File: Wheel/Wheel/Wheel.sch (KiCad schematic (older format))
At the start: 118 parts, among them J1 Conn_02x09_Odd_Even, J10 RJ45, J11 Screw_Terminal_01x02, J12 DS-201, J13 Conn_01x04, J14 Conn_02x13_Top_Bottom, J15 DB25_Female, J16 Conn_01x06, J17 Conn_01x07, J18 Conn_01x06, J19 RJ45, J2 RJ45, J20 DB9_Male, J21 DB9_Female, J3 RJ45, J4 RJ45, J5 USB_B, J6 Conn_02x09_Odd_Even, J7 Conn_02x10_Odd_Even, J8 RJ45, J9 RJ45, U1 MCP23S17_SP, U10 PC817, U11 PC817, U12 IP4220CZ6, U15 PC817, U2 STM32F407VETx, U3 USBLC6-2SC6, U4 IP4220CZ6, U5 MCP23S17_SP, U6 AMS1117, U7 4N35, U8 PC817, U9 PC817, Y1 32,768 кГц, Y2 8MHz

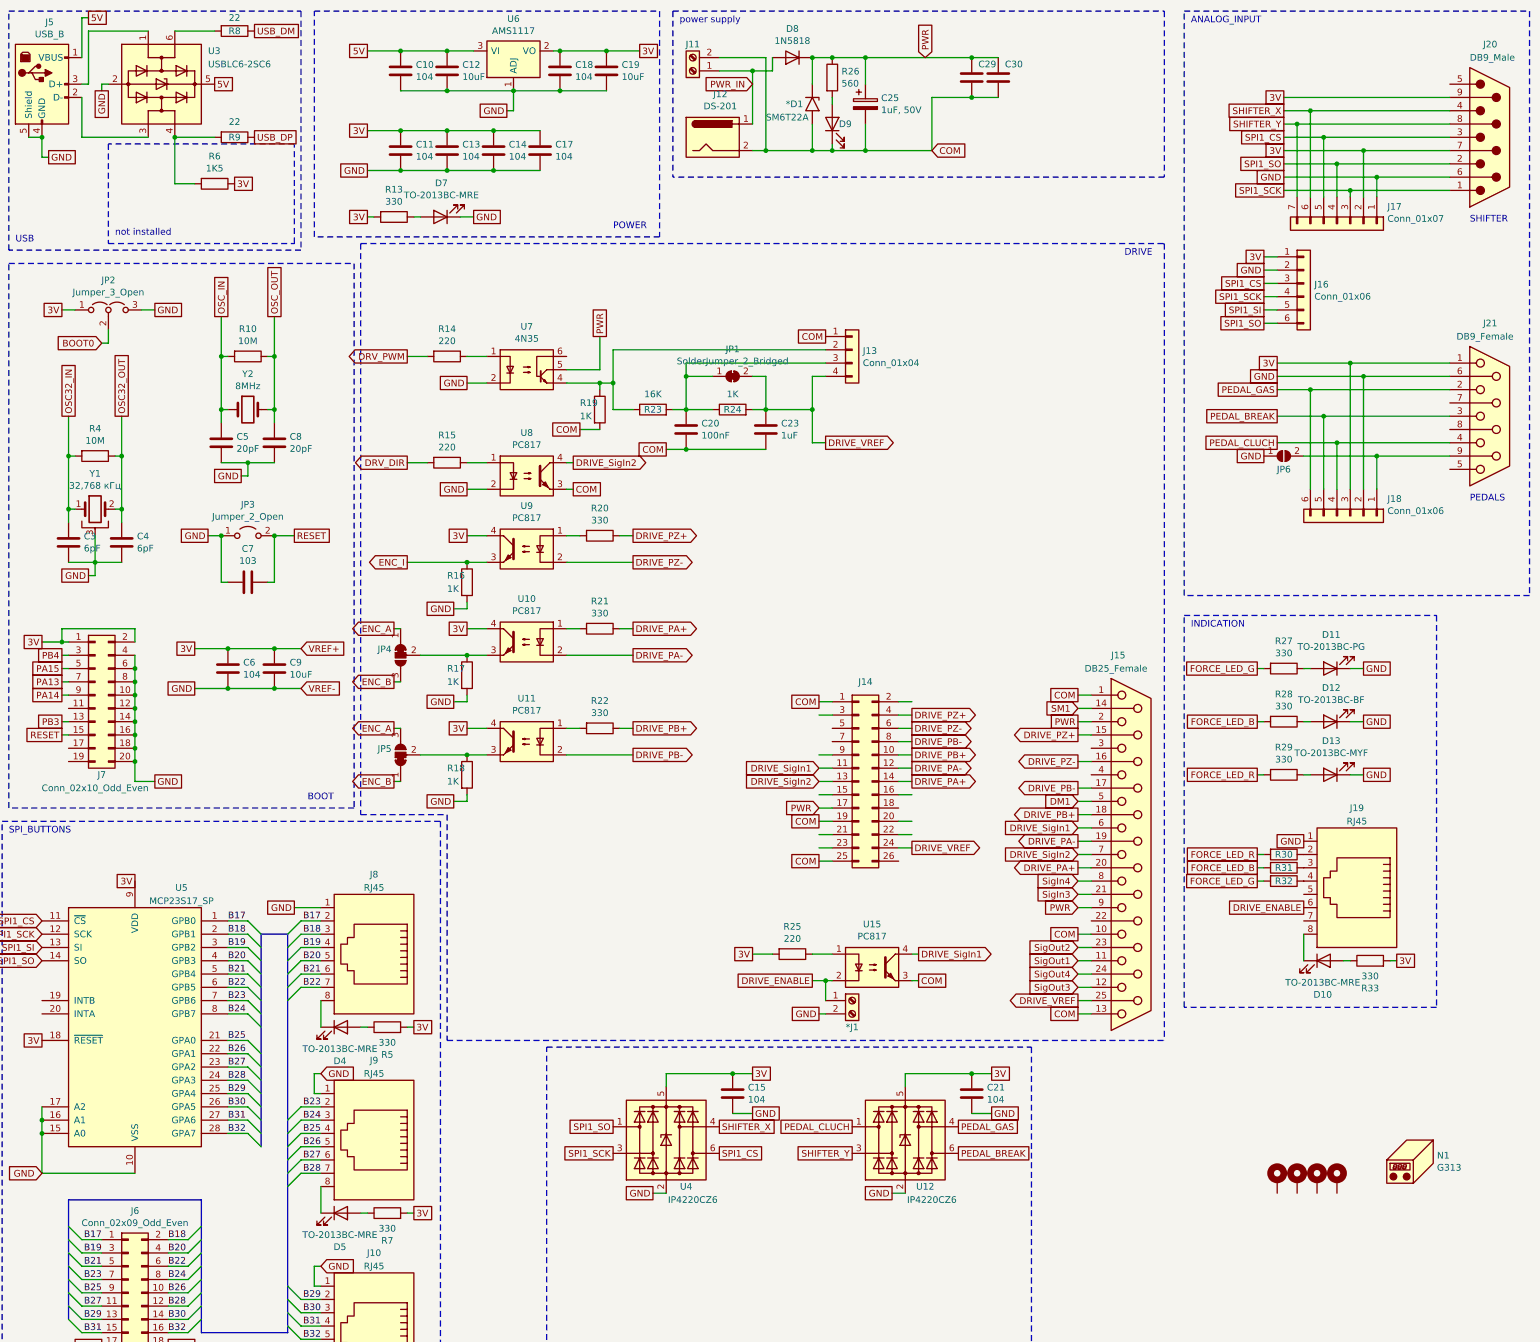
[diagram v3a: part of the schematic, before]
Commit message: Wheel's PCB changed
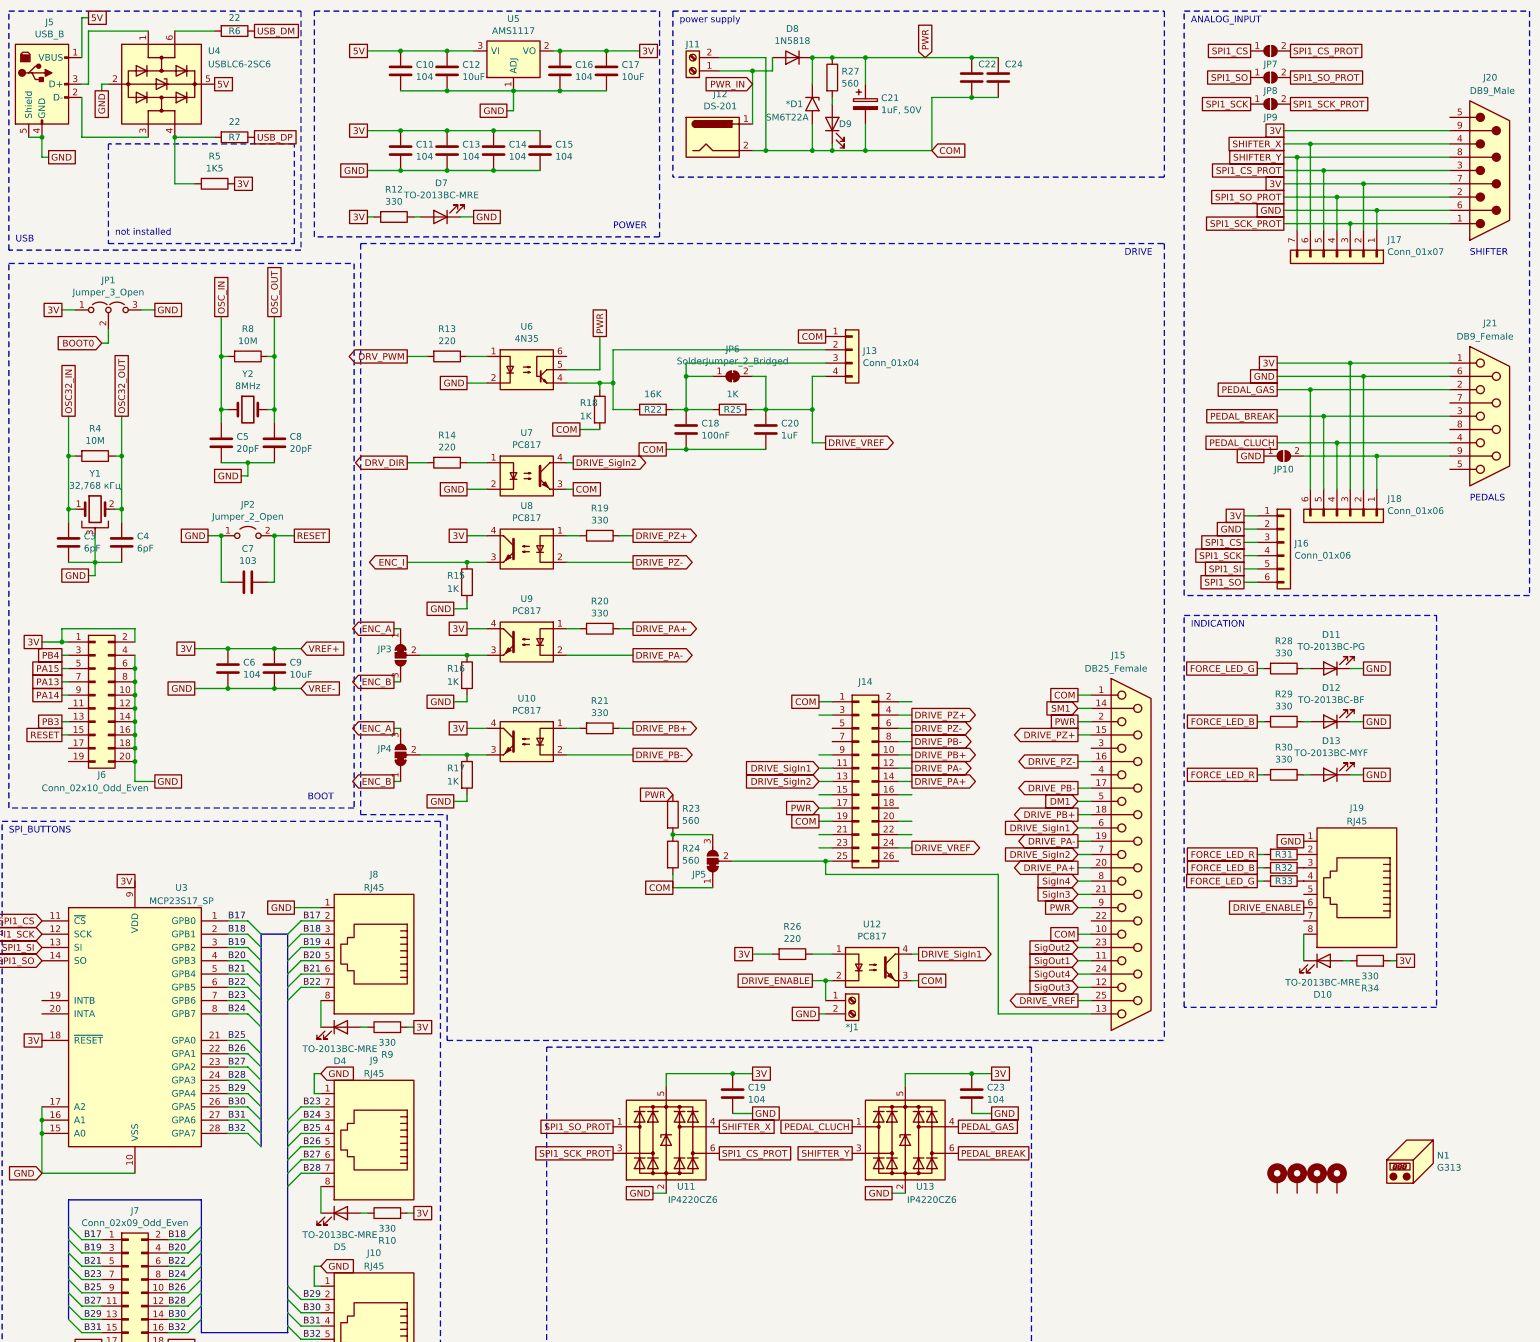
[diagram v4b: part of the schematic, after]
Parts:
- added JP5: SolderJumper_3_Bridged12, Jumper:SolderJumper-3_P1.3mm_Bridged12_RoundedPad1.0x1.5mm, symbol Jumper:SolderJumper_3_Bridged12
- added JP7, JP8, JP9: SolderJumper_2_Open, Jumper:SolderJumper-2_P1.3mm_Open_RoundedPad1.0x1.5mm, symbol Jumper:SolderJumper_2_Open
- added R23, R24: 560, Resistor_SMD:R_0805_2012Metric, symbol Device:R
- renumbered C17 to C15, C18 to C16, C19 to C17, C20 to C18, C15 to C19, C23 to C20, C25 to C21, C29 to C22, C21 to C23, C30 to C24, J7 to J6, J6 to J7, JP2 to JP1, JP6 to JP10, JP3 to JP2, JP4 to JP3, JP5 to JP4, JP1 to JP6, R7 to R10, R13 to R12, R14 to R13, R15 to R14, R16 to R15, R17 to R16, R18 to R17, R19 to R18, R20 to R19, R21 to R20, R22 to R21, R23 to R22, R24 to R25, R25 to R26, R26 to R27, R27 to R28, R28 to R29, R29 to R30, R30 to R31, R31 to R32, R32 to R33, R33 to R34, R6 to R5, R8 to R6, R9 to R7, R10 to R8, R5 to R9, U11 to U10, U4 to U11, U15 to U12, U12 to U13, U5 to U3, U3 to U4, U6 to U5, U7 to U6, U8 to U7, U9 to U8, U10 to U9
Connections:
- net COM: now also JP5.1 (A), R24.2; no longer J14.25 (Pin_25), J15.13
- net PWR: now also R23.1
- net SPI1_CS: now also JP7.1 (A); no longer J17.5 (Pin_5), J20.3, U11.6 (I/O4)
- net SPI1_SCK: now also JP9.1 (A); no longer J17.3 (Pin_3), J20.1, U11.3 (I/O2)
- net SPI1_SO: now also JP8.1 (A); no longer J17.4 (Pin_4), J20.2, U11.1 (I/O1)
- new net: J14.25 (Pin_25), J15.13, JP5.2 (C)
- new net: JP5.3 (B), R23.2, R24.1
- new net SPI1_CS_PROT: J17.5 (Pin_5), J20.3, JP7.2 (B), U11.6 (I/O4)
- new net SPI1_SCK_PROT: J17.3 (Pin_3), J20.1, JP9.2 (B), U11.3 (I/O2)
- new net SPI1_SO_PROT: J17.4 (Pin_4), J20.2, JP8.2 (B), U11.1 (I/O1)
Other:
- moved on the sheet: J16, J17, J20
